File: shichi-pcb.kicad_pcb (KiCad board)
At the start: 2 copper layers, 266 x 96 mm, 176 parts, among them J1 USB_C_Receptacle_HRO_TYPE-C-3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, J2 Conn_01x04_Male, J3 Conn_01x06_Male, J4 Conn_01x04_Male, J5 Conn_01x02_Male, J6 Conn_01x01_Male, K1 SW_Push, K10 SW_Push, K11 SW_Push, K12 SW_Push, K13 SW_Push, K14 SW_Push, K15 SW_Push, K16 SW_Push, K17 SW_Push, K18 SW_Push, K19 SW_Push, K2 SW_Push, K20 SW_Push, K21 SW_Push, K22 SW_Push, K23 SW_Push, K24 SW_Push, K25 SW_Push, K26 SW_Push, K27 SW_Push, K28 SW_Push, K29 SW_Push, K3 SW_Push, K30 SW_Push, K31 SW_Push, K32 SW_Push, K33 SW_Push, K34 SW_Push, K35 SW_Push, K36 SW_Push, K37 SW_Push, K38 SW_Push, K39 SW_Push, K4 SW_Push, K40 SW_Push, K41 SW_Push, K42 SW_Push, K43 SW_Push, K44 SW_Push, K45 SW_Push, K46 SW_Push, K47 SW_Push, K48 SW_Push, K49 SW_Push, K5 SW_Push, K50 SW_Push, K51 SW_Push, K52 SW_Push, K53 SW_Push, K54 SW_Push, K55 SW_Push, K56 SW_Push, K57 SW_Push, K58 SW_Push, K59 SW_Push, K6 SW_Push, K60 SW_Push, K61 SW_Push, K62 SW_Push, K63 SW_Push, K64 SW_Push, K65 SW_Push, K66 SW_Push, K67 SW_Push, K68 SW_Push, K69 SW_Push, K7 SW_Push, K70 SW_Push, K71 SW_Push, K72 SW_Push, K8 SW_Push, K9 SW_Push, SW1 SW_Push, SW2 SW_Push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

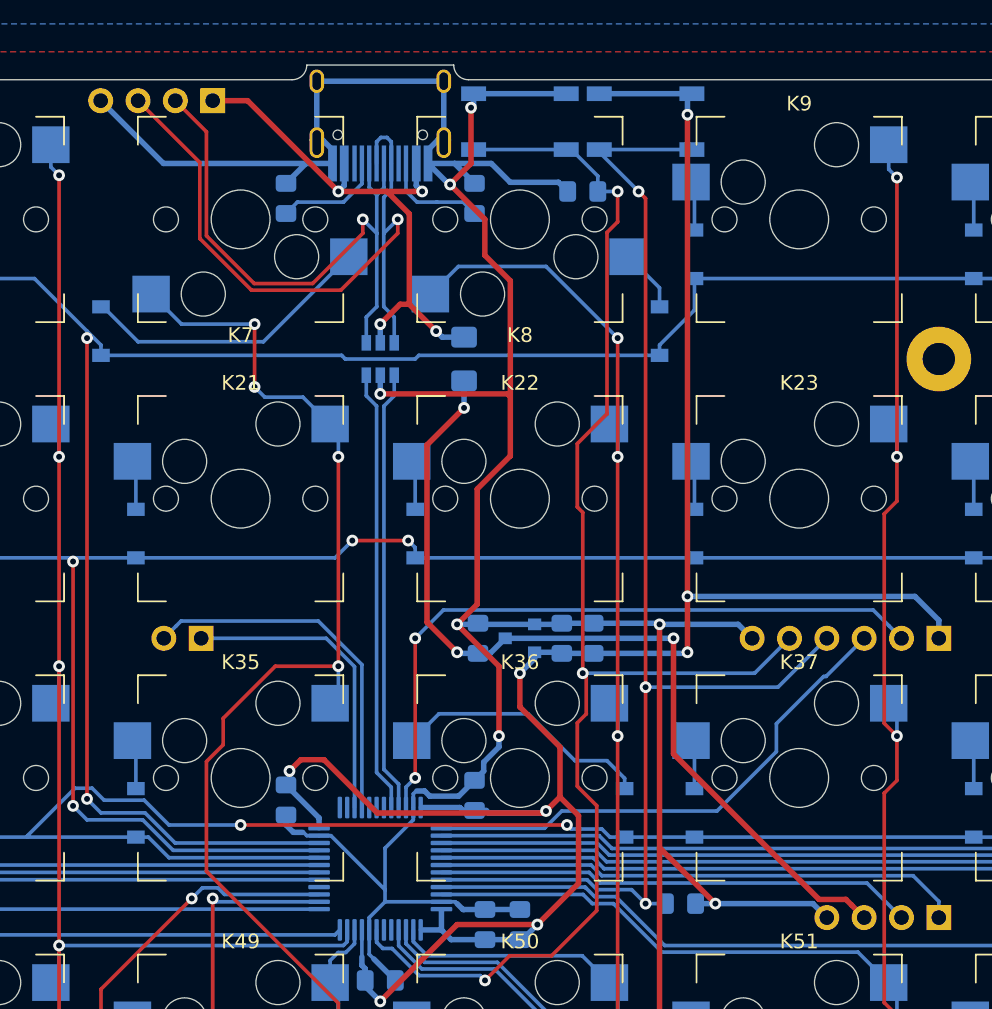
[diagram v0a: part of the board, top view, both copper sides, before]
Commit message: Remove USB headers
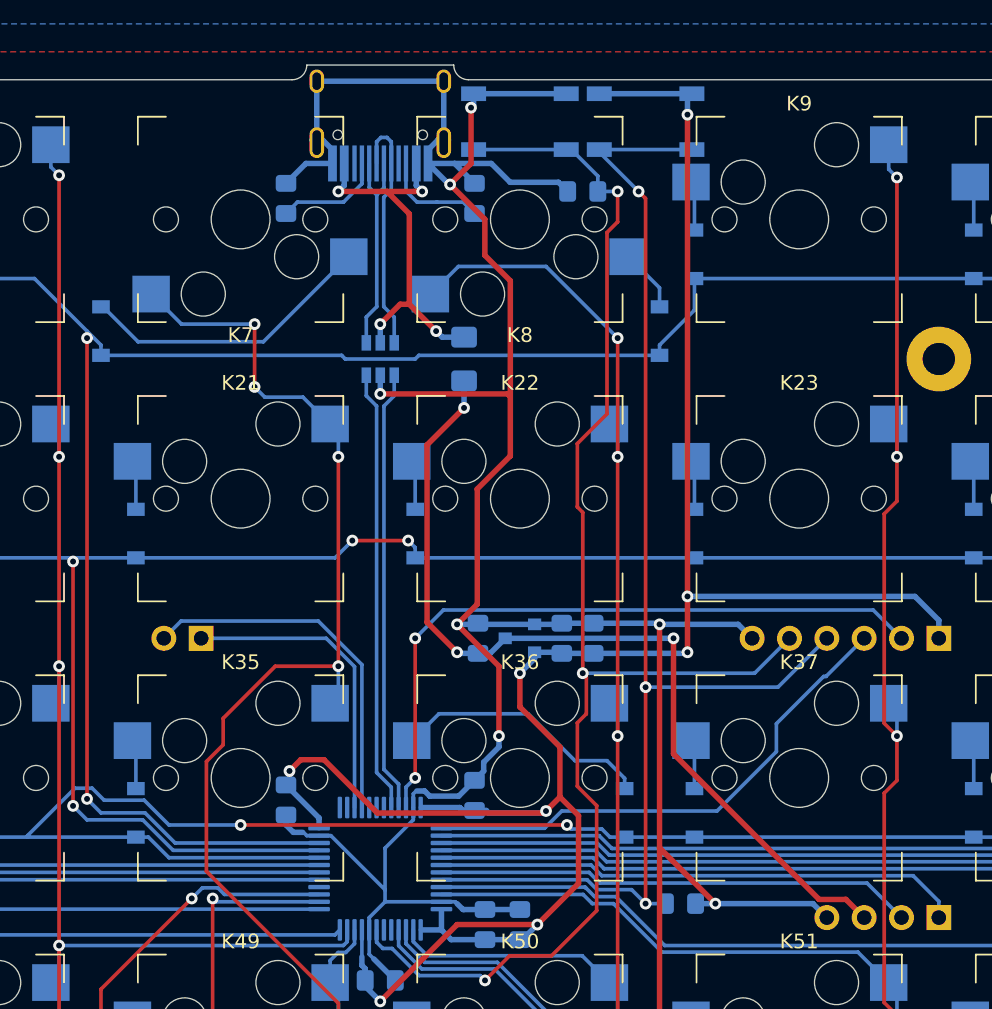
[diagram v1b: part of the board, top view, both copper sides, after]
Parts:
- removed the J2 at (171.6, 51.4)
- renumbered J3 to J2, J4 to J3, J5 to J4, J6 to J5
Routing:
- net D+Bus: track 46.8 -> 16.9 mm, vias 1 -> 0
- net D-Bus: track 40.8 -> 15.1 mm, vias 1 -> 0
- net GND: track 250.2 -> 234.5 mm
- net VCC: track 37.7 -> 26.6 mm
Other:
- board text removed: "D+"
- board text removed: "D-"
- board text removed: "VCC"

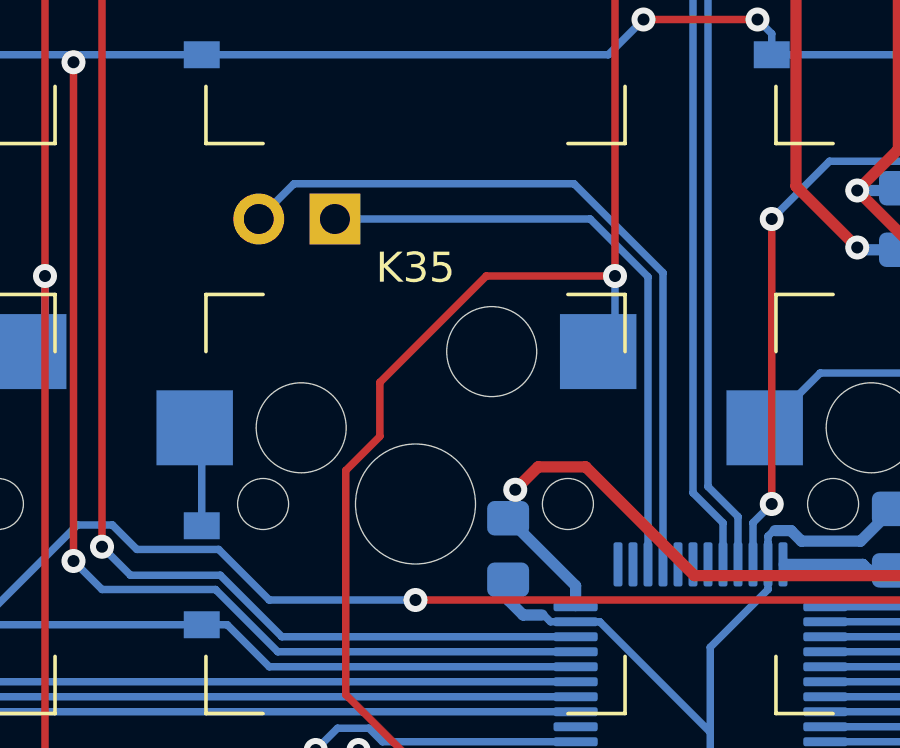
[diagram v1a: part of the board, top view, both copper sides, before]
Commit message: Remove B14 and B15 pin headers
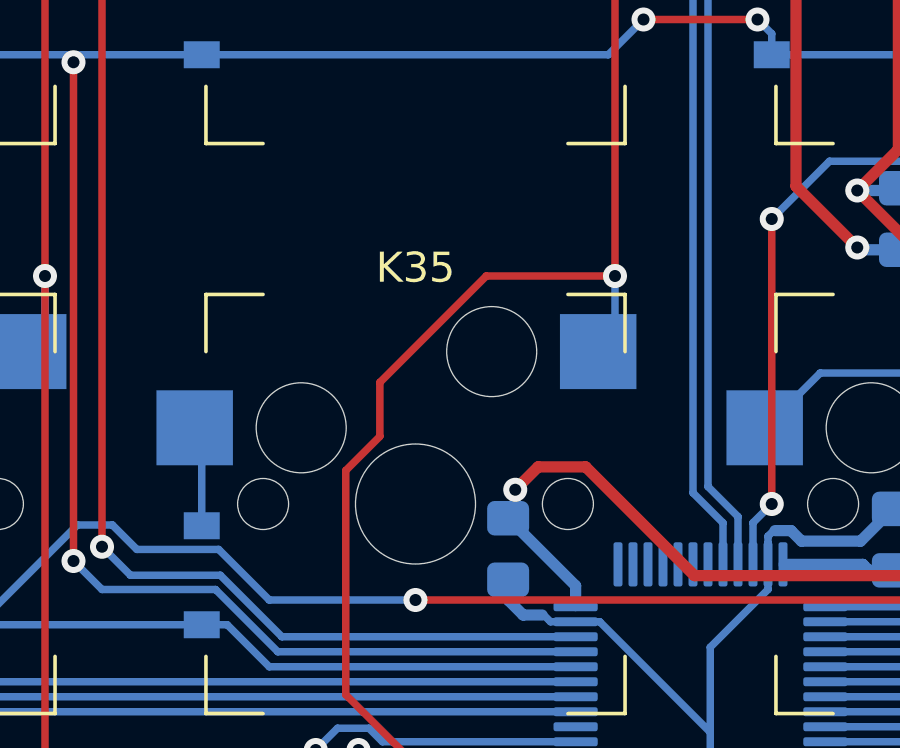
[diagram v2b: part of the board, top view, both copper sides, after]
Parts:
- removed J4: Conn_01x02_Male, Connector_PinSocket_2.54mm:PinSocket_1x02_P2.54mm_Vertical
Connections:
- U3 pad 27: B14 -> Net-(U3-Pad27)
- U3 pad 28: B15 -> Net-(U3-Pad28)
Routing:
- net B15: track 24.9 -> 0.00 mm
- net B14: track 20.8 -> 0.00 mm
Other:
- board text removed: "B14"
- board text removed: "B15"
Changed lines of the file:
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@@
   (general
     (thickness 1.6)
-    (drawings 35)
-    (tracks 1001)
+    (drawings 33)
+    (tracks 994)
     (zones 0)
-    (modules 175)
+    (modules 174)
     (nets 121)
   )
@@
   (net 117 "Net-(U3-Pad29)")
   (net 118 "Net-(U3-Pad25)")
-  (net 119 B15)
-  (net 120 B14)
+  (net 119 "Net-(U3-Pad28)")
+  (net 120 "Net-(U3-Pad27)")
   (net_class Default "This is the default net class."
     (clearance 0.2)
@@
     (add_net AUDIO_0)
     (add_net AUDIO_1)
-    (add_net B14)
-    (add_net B15)
     (add_net BOOT0)
     (add_net COL0)
@@
     (add_net "Net-(U3-Pad25)")
     (add_net "Net-(U3-Pad26)")
+    (add_net "Net-(U3-Pad27)")
+    (add_net "Net-(U3-Pad28)")
     (add_net "Net-(U3-Pad29)")
     (add_net "Net-(U3-Pad30)")
@@
       (net 117 "Net-(U3-Pad29)"))
     (pad 28 smd roundrect (at 4.1625 -1.25 90) (size 1.475 0.3) (layers B.Cu B.Paste B.Mask) (roundrect_rratio 0.25)
-      (net 119 B15))
+      (net 119 "Net-(U3-Pad28)"))
     (pad 27 smd roundrect (at 4.1625 -1.75 90) (size 1.475 0.3) (layers B.Cu B.Paste B.Mask) (roundrect_rratio 0.25)
-      (net 120 B14))
+      (net 120 "Net-(U3-Pad27)"))
     (pad 26 smd roundrect (at 4.1625 -2.25 90) (size 1.475 0.3) (layers B.Cu B.Paste B.Mask) (roundrect_rratio 0.25)
       (net 116 "Net-(U3-Pad26)"))
@@
     )
   )
-  (module Connector_PinSocket_2.54mm:PinSocket_1x02_P2.54mm_Vertical (layer B.Cu)
-    (at 170.815 88 90)
-    (descr "Through hole straight socket strip, 1x02, 2.54mm pitch, single row (from Kicad 4.0.7), script generated")
-    (tags "Through hole socket strip THT 1x02 2.54mm single row")
-    (fp_text reference J4 (at 0 2.77 270) (layer B.SilkS)
-      (effects (font (size 1 1) (thickness 0.15)) (justify mirror))
-    )
-    (fp_text value Conn_01x02_Male (at 0 -5.31 270) (layer B.Fab)
-      (effects (font (size 1 1) (thickness 0.15)) (justify mirror))
-    )
-    (fp_text user %R (at 0 -1.27) (layer B.Fab)
-      (effects (font (size 1 1) (thickness 0.15)) (justify mirror))
-    )
-    (fp_line (start -1.8 -4.3) (end -1.8 1.8) (layer B.CrtYd) (width 0.05))
-    (fp_line (start 1.75 -4.3) (end -1.8 -4.3) (layer B.CrtYd) (width 0.05))
-    (fp_line (start 1.75 1.8) (end 1.75 -4.3) (layer B.CrtYd) (width 0.05))
-    (fp_line (start -1.8 1.8) (end 1.75 1.8) (layer B.CrtYd) (width 0.05))
-    (fp_line (start 0 1.33) (end 1.33 1.33) (layer B.SilkS) (width 0.12))
-    (fp_line (start 1.33 1.33) (end 1.33 0) (layer B.SilkS) (width 0.12))
-    (fp_line (start 1.33 -1.27) (end 1.33 -3.87) (layer B.SilkS) (width 0.12))
-    (fp_line (start -1.33 -3.87) (end 1.33 -3.87) (layer B.SilkS) (width 0.12))
-    (fp_line (start -1.33 -1.27) (end -1.33 -3.87) (layer B.SilkS) (width 0.12))
-    (fp_line (start -1.33 -1.27) (end 1.33 -1.27) (layer B.SilkS) (width 0.12))
-    (fp_line (start -1.27 -3.81) (end -1.27 1.27) (layer B.Fab) (width 0.1))
-    (fp_line (start 1.27 -3.81) (end -1.27 -3.81) (layer B.Fab) (width 0.1))
-    (fp_line (start 1.27 0.635) (end 1.27 -3.81) (layer B.Fab) (width 0.1))
-    (fp_line (start 0.635 1.27) (end 1.27 0.635) (layer B.Fab) (width 0.1))
-    (fp_line (start -1.27 1.27) (end 0.635 1.27) (layer B.Fab) (width 0.1))
-    (pad 2 thru_hole oval (at 0 -2.54 90) (size 1.7 1.7) (drill 1) (layers *.Cu *.Mask)
-      (net 119 B15))
-    (pad 1 thru_hole rect (at 0 0 90) (size 1.7 1.7) (drill 1) (layers *.Cu *.Mask)
-      (net 120 B14))
-    (model ${KISYS3DMOD}/Connector_PinSocket_2.54mm.3dshapes/PinSocket_1x02_P2.54mm_Vertical.wrl
-      (at (xyz 0 0 0))
-      (scale (xyz 1 1 1))
-      (rotate (xyz 0 0 0))
-    )
-  )
   (module Connector_PinSocket_2.54mm:PinSocket_1x04_P2.54mm_Vertical (layer B.Cu)
     (at 221 107 90)
@@
     (effects (font (size 1 1) (thickness 0.15)) (justify mirror))
   )
-  (gr_text B15 (at 168.275 90) (layer B.SilkS)
-    (effects (font (size 0.6 0.6) (thickness 0.125)) (justify mirror))
-  )
-  (gr_text B14 (at 170.815 90) (layer B.SilkS)
-    (effects (font (size 0.6 0.6) (thickness 0.125)) (justify mirror))
-  )
   (gr_text A5 (at 168.275 128) (layer B.SilkS)
     (effects (font (size 0.6 0.6) (thickness 0.125)) (justify mirror))
@@
   (segment (start 189.175 55.7) (end 187.75 57.125) (width 0.375) (layer F.Cu) (net 1))
   (segment (start 189.175 51.9) (end 189.175 55.7) (width 0.375) (layer F.Cu) (net 1))
-  (segment (start 177.9425 55.695) (end 176.5875 57.05) (width 0.375) (layer B.Cu) (net 1))
-  (segment (start 179.75 55.695) (end 177.9425 55.695) (width 0.375) (layer B.Cu) (net 1))
+  (segment (start 177.9425 55.695) (end 176.5875 57.05) (width 0.375) (layer B.Cu) (net 1) (status 20))
+  (segment (start 179.75 55.695) (end 177.9425 55.695) (width 0.375) (layer B.Cu) (net 1) (status 10))
   (via (at 180.15 57.599999) (size 0.8) (drill 0.4) (layers F.Cu B.Cu) (net 2))
   (segment (start 180.55 55.695) (end 180.55 57.199999) (width 0.375) (layer B.Cu) (net 2) (status 10))
@@
   (segment (start 175.475 122.2) (end 175.875 122.6) (width 0.25) (layer B.Cu) (net 110) (status 30))
   (segment (start 174.45 122.2) (end 175.475 122.2) (width 0.25) (layer B.Cu) (net 110) (status 20))
-  (segment (start 181.75 99.5125) (end 181.75 89.790588) (width 0.25) (layer B.Cu) (net 119) (status 10))
-  (segment (start 169.450001 86.824999) (end 168.275 88) (width 0.25) (layer B.Cu) (net 119) (status 20))
-  (segment (start 178.784411 86.824999) (end 169.450001 86.824999) (width 0.25) (layer B.Cu) (net 119))
-  (segment (start 181.75 89.790588) (end 178.784411 86.824999) (width 0.25) (layer B.Cu) (net 119))
-  (segment (start 181.25 99.5125) (end 181.25 89.926998) (width 0.25) (layer B.Cu) (net 120) (status 10))
-  (segment (start 181.25 89.926998) (end 179.323002 88) (width 0.25) (layer B.Cu) (net 120))
-  (segment (start 179.323002 88) (end 170.815 88) (width 0.25) (layer B.Cu) (net 120) (status 20))
   (zone (net 1) (net_name GND) (layer F.Cu) (hatch edge 0.508)
     (connect_pads (clearance 0.508))

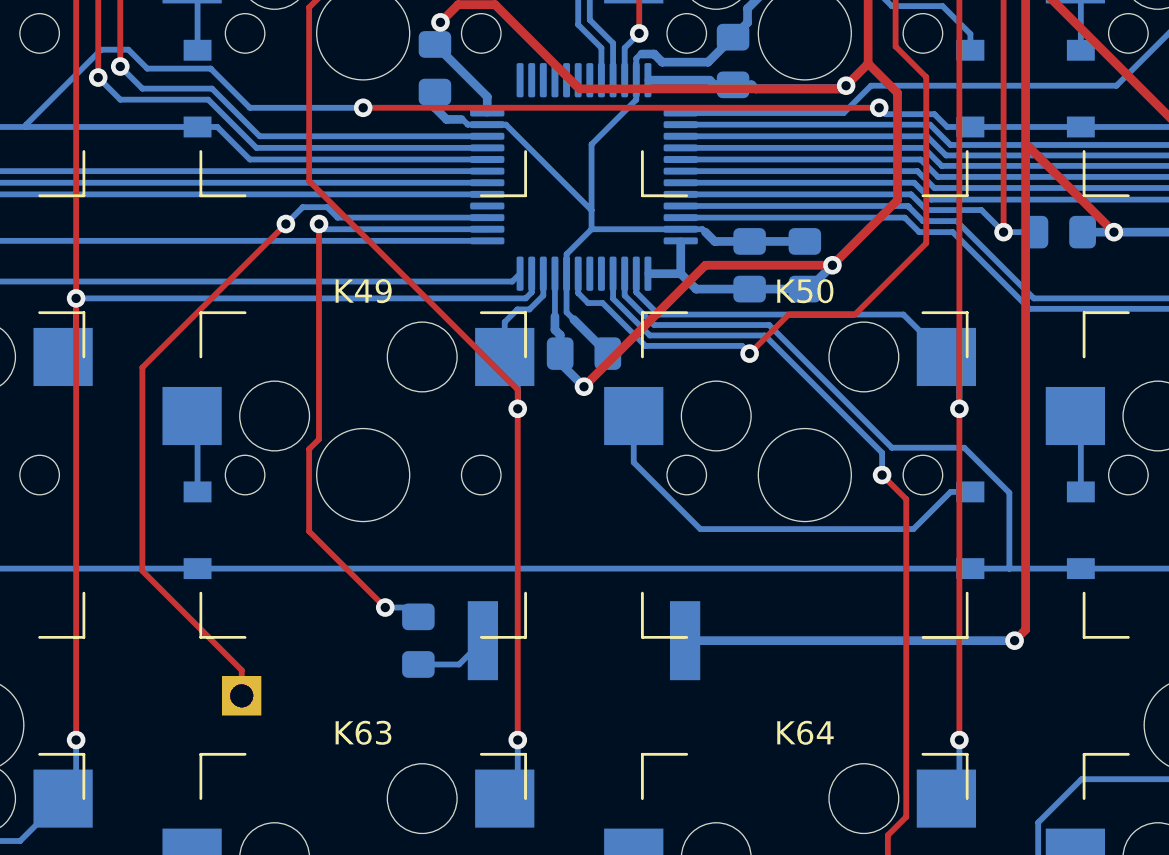
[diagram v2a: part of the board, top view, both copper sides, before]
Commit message: Remove AUDIO components
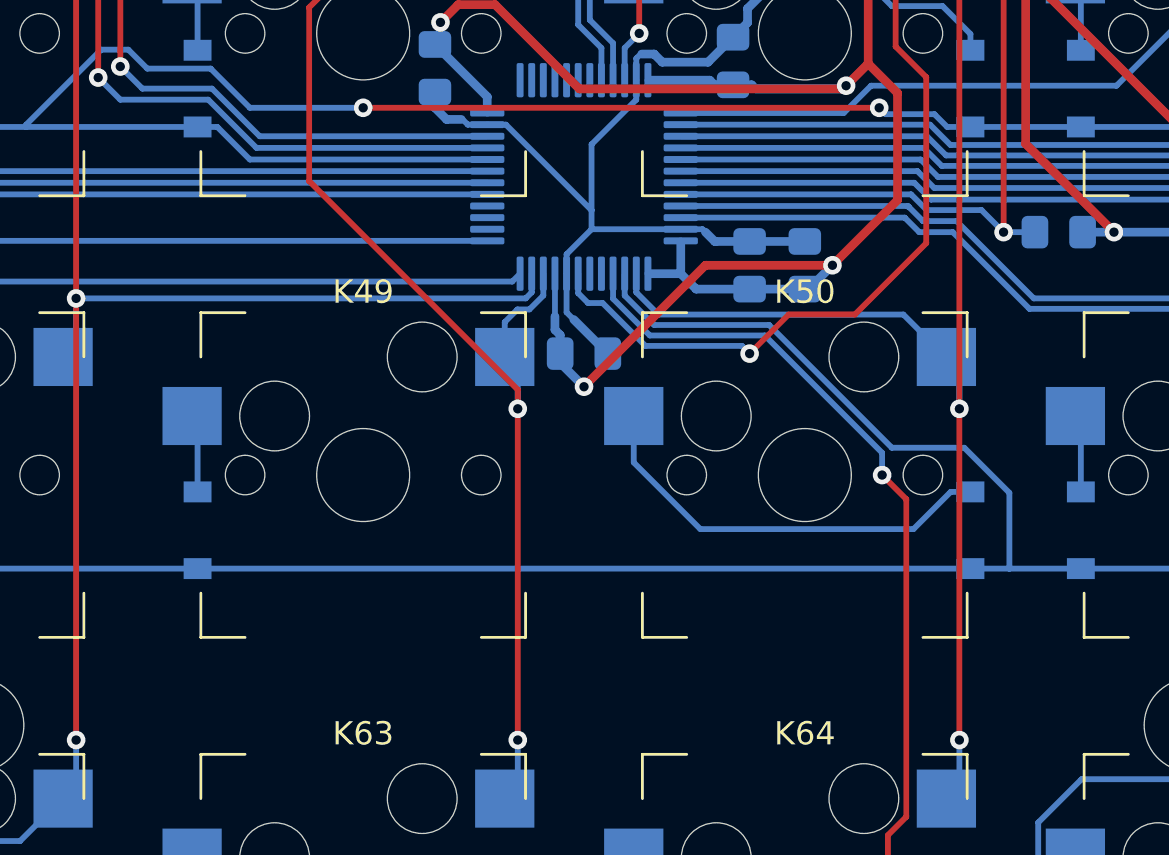
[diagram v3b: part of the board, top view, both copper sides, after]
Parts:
- removed BZ1: Buzzer, Buzzer_Beeper:Buzzer_Murata_PKMCS0909E4000-R1
- removed J5: Conn_01x01_Male, Connector_PinSocket_2.54mm:PinSocket_1x01_P2.54mm_Vertical
- removed R4: 1k, Resistor_SMD:R_0805_2012Metric_Pad1.15x1.40mm_HandSolder
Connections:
- U3 pad 14: AUDIO_0 -> Net-(U3-Pad14)
- U3 pad 15: AUDIO_1 -> Net-(U3-Pad15)
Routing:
- net GND: track 234.5 -> 198.7 mm, vias 8 -> 7
- net AUDIO_1: track 33.8 -> 0.00 mm, vias 1 -> 0
- net AUDIO_0: track 27.0 -> 0.00 mm, vias 2 -> 0
- net Net-(BZ1-Pad1): track 3.20 -> 0.00 mm
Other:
- board text removed: "A5"

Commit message: Update PCB layout design to v2
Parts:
- removed J2: Conn_01x06_Male, Connector_PinSocket_2.54mm:PinSocket_1x06_P2.54mm_Vertical
- removed J3: Conn_01x04_Male, Connector_PinSocket_2.54mm:PinSocket_1x04_P2.54mm_Vertical
- removed SW1, SW2: SW_Push, Button_Switch_SMD:SW_SPST_TL3342
- added BOOT0: SW_Push, Button_Switch_SMD:SW_SPST_TL3342, B.Cu at (306.5, 107.0)
- added I2C1: Conn_01x04_Male, Miscellaneous_Keyboard_Parts:I2C_Header_1x04_P2.54mm_Vertical, B.Cu at (297.0, 130.4)
- added NRST: SW_Push, Button_Switch_SMD:SW_SPST_TL3342, B.Cu at (306.5, 88.0)
- added SWD1: Conn_01x05_Male, Miscellaneous_Keyboard_Parts:SWD_Header_1x05_P2.54mm_Vertical, B.Cu at (301.4, 126.0)
- C3: value 1uF -> 4.7uF
- K1, K10, K11, K12, K13, K14, K15, K16, K17, K18, K19, K2, K20, K21, K22, K23, K24, K25, K26, K27, K28, K29, K3, K30, K31, K32, K33, K34, K35, K36, K37, K38, K39, K4, K40, K41, K42, K43, K44, K45, K46, K47, K48, K49, K5, K50, K51, K52, K53, K54, K55, K56, K57, K58, K59, K6, K60, K61, K63, K64, K65, K66, K67, K68, K69, K7, K70, K8, K9: footprint MX_Switch:SW_Cherry_MX_1.00u_PCB_Socket -> MX_Switch:MX_1.00u_PCB
- K62: footprint MX_Switch:SW_Cherry_MX_1.00u_PCB_Socket -> MX_Switch:MX_7.00u_PCB_ReversedStabilizers
- K71, K72: footprint MX_Switch:SW_Cherry_MX_2.00u_PCB_Socket -> MX_Switch:MX_2.00u_PCB_ReversedStabilizers
- U2: value USBLC6-2SC6 -> PRTR5V0U2X; footprint Package_TO_SOT_SMD:SOT-23-6 -> Package_TO_SOT_SMD:SOT-143
- moved C2 108.8 mm to (301.3, 88.0), turned to 90 degrees
- moved R1 97.8 mm to (274.2, 64.2), turned to 90 degrees
- moved U2 95.1 mm to (278.0, 64.2), turned to 180 degrees
- moved J1 95.0 mm to (278.0, 45.0)
- moved U3 95.0 mm to (278.0, 105.6)
- moved C9 94.8 mm to (271.4, 101.8)
- moved C7 94.5 mm to (284.6, 109.4)
- moved C4 94.1 mm to (286.6, 109.4)
- moved C5 94.0 mm to (277.0, 113.2)
- moved C8 93.4 mm to (282.8, 100.3)
- moved F1 93.1 mm to (281.8, 69.0)
- moved C3 92.6 mm to (288.0, 87.5)
- moved R2 92.6 mm to (281.8, 64.2), turned to 270 degrees
- moved U1 92.2 mm to (284.6, 87.5)
- moved C1 91.7 mm to (281.3, 87.5)
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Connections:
- J1 pad A6: D+Bus -> D+
- J1 pad A7: D-Bus -> D-
- J1 pad B6: D+Bus -> D+
- J1 pad B7: D-Bus -> D-
- K71 pad 1: COL5 -> COL4
- K71 pad 2: Net-(D62-Pad2) -> Net-(D61-Pad2)
- K72 pad 1: COL8 -> COL6
- K72 pad 2: Net-(D65-Pad2) -> Net-(D63-Pad2)
- U2 pad 1: D+ -> GND
- U2 pad 2: GND -> D+
- U2 pad 4: D-Bus -> VCC
- U3 pad 10: COL6 -> COL13
- U3 pad 11: COL5 -> COL12
- U3 pad 12: COL4 -> ROW4
- U3 pad 13: COL3 -> ROW3
- U3 pad 14: Net-(U3-Pad14) -> COL11
- U3 pad 15: Net-(U3-Pad15) -> ROW2
- U3 pad 16: Net-(U3-Pad16) -> ROW1
- U3 pad 17: COL2 -> ROW0
- U3 pad 18: COL1 -> COL10
- U3 pad 19: COL0 -> COL9
- U3 pad 2: COL7 -> Net-(U3-Pad2)
- U3 pad 20: ROW2 -> COL8
- U3 pad 21: ROW1 -> COL7
- U3 pad 22: ROW0 -> COL6
- U3 pad 25: Net-(U3-Pad25) -> COL5
- U3 pad 26: Net-(U3-Pad26) -> COL4
- U3 pad 27: Net-(U3-Pad27) -> COL3
- U3 pad 28: Net-(U3-Pad28) -> COL2
- U3 pad 29: Net-(U3-Pad29) -> COL1
- U3 pad 3: ROW3 -> Net-(U3-Pad3)
- U3 pad 30: Net-(U3-Pad30) -> COL0
- U3 pad 38: COL13 -> Net-(U3-Pad38)
- U3 pad 39: COL12 -> Net-(U3-Pad39)
- U3 pad 4: ROW4 -> Net-(U3-Pad4)
- U3 pad 40: COL11 -> Net-(U3-Pad40)
- U3 pad 41: COL10 -> Net-(U3-Pad41)
- U3 pad 45: COL9 -> Net-(U3-Pad45)
- U3 pad 46: COL8 -> Net-(U3-Pad46)
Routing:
- net COL6: track 95.6 -> 357.3 mm, vias 6 -> 0
- net COL4: track 123.0 -> 366.7 mm, vias 5 -> 0
- net COL5: track 133.6 -> 373.2 mm, vias 5 -> 0
- net COL3: track 141.1 -> 337.5 mm, vias 5 -> 0
- net COL7: track 102.1 -> 290.8 mm, vias 5 -> 0
- net COL2: track 161.0 -> 320.6 mm, vias 5 -> 0
- net COL1: track 180.2 -> 305.2 mm, vias 5 -> 0
- net COL0: track 199.4 -> 320.3 mm, vias 5 -> 0
- net COL11: track 175.1 -> 85.8 mm, vias 5 -> 0
- net COL12: track 194.3 -> 108.8 mm, vias 5 -> 0
- net COL13: track 213.5 -> 130.3 mm, vias 5 -> 0
- net COL8: track 154.0 -> 232.9 mm, vias 5 -> 0
- net BOOT0: track 88.5 -> 29.7 mm, vias 3 -> 0
- net COL9: track 136.1 -> 176.9 mm, vias 5 -> 0
- net +5V: track 61.0 -> 22.1 mm, vias 3 -> 0
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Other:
- board size 266 x 96 mm -> 287 x 116 mm
- board text removed: "3.3V"
- board text removed: "5V"
- board text removed: "BT0"
- board text removed: "CLK"
- board text removed: "DIO"
- board text removed: "GND"
- board text removed: "NRST"
- board text removed: "SCL"
- board text removed: "SDA"
